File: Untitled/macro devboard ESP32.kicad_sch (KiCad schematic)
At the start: 48 parts, among them J1 12402012E212A, J2 Conn_01x02_Pin, J3 Conn_02x04_Odd_Even, Q1 BSS84LT1G, SW1 MX_SW_HS, SW3 RST, SW6 MX_SW_HS, SW7 MX_SW_HS, SW8 MX_SW_HS, SW9 MX_SW_HS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

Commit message: used keypad, which doesn't work
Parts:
- removed J2: Conn_01x02_Pin, Connector_JST:JST_XH_B2B-XH-A_1x02_P2.50mm_Vertical, symbol Connector:Conn_01x02_Pin
- added C1: 100nF, Capacitor_SMD:C_0603_1608Metric_Pad1.08x0.95mm_HandSolder, symbol Device:C
- added J4: Conn_01x02_Pin, Connector_JST:JST_PH_S2B-PH-K_1x02_P2.00mm_Horizontal, symbol Connector:Conn_01x02_Pin
- added SW2: 1825232-1, 1825232-1:1825232-1_TEC, symbol 2025-07-25_23-02-08:OS102011MA1QN1
- added TP1: VBAT, TestPoint:TestPoint_Pad_D2.0mm, symbol Connector:TestPoint
- added TP2: GND, TestPoint:TestPoint_Pad_D2.0mm, symbol Connector:TestPoint
- added TP3: EN, TestPoint:TestPoint_Pad_D2.0mm, symbol Connector:TestPoint
- added TP4: VBUS, TestPoint:TestPoint_Pad_D2.0mm, symbol Connector:TestPoint
- added TP5: VDD, TestPoint:TestPoint_Pad_D2.0mm, symbol Connector:TestPoint
- added TP6: VIN, TestPoint:TestPoint_Pad_D2.0mm, symbol Connector:TestPoint
- R14: value 2.7k -> PROG
- SW1, SW6, SW7, SW8, SW9: footprint keyswitches:Kailh_socket_MX -> keyswitches:Kailh_socket_MX_optional
- U4: footprint Package_TO_SOT_SMD:SOT-23-5 -> Package_TO_SOT_SMD:SC-74A-5_1.55x2.9mm_P0.95mm
- renumbered JP11 to LED0, JP10 to LED1
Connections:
- net EN: now also TP3.1
- net GND: now also C1.2, J4.2 (Pin_2), TP2.1
- net VBAT: now also SW2.1, SW2.2
- net VBUS: now also C1.1, TP4.1
- net VDD: now also TP5.1
- net at C3.2, C4.2, D11.1 (K)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: now also TP6.1
- new net VBAT_IN: J4.1 (Pin_1), SW2.3, TP1.1
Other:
- note added: "A compact 2X3 macro pad devboard, powered by the ESP32-C3. FEATURES: - 5 key switches, 1 rotary encoder - 8 accessible IO header pins - 2 controllable LEDs (optional) - USB-C interface, with ESD protection - Battery Charging"
- note added: "Battery Charging Management"
- note added: "IO"
- note added: "Mounting"
- note removed: "This is a macro-pad that also works as a dev board, based on the nRF52840 to teach myself about Quarq's HW workflow. FEATURES: - 6 key switches, 1 rotary encoder - 26 accessible IO header pins - USB-C interface, with ESD protection - Antenna"
- moved on the sheet: C8, C9, D10, D12, D8, D9, H1, H2, J1, J3, LED0, LED1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

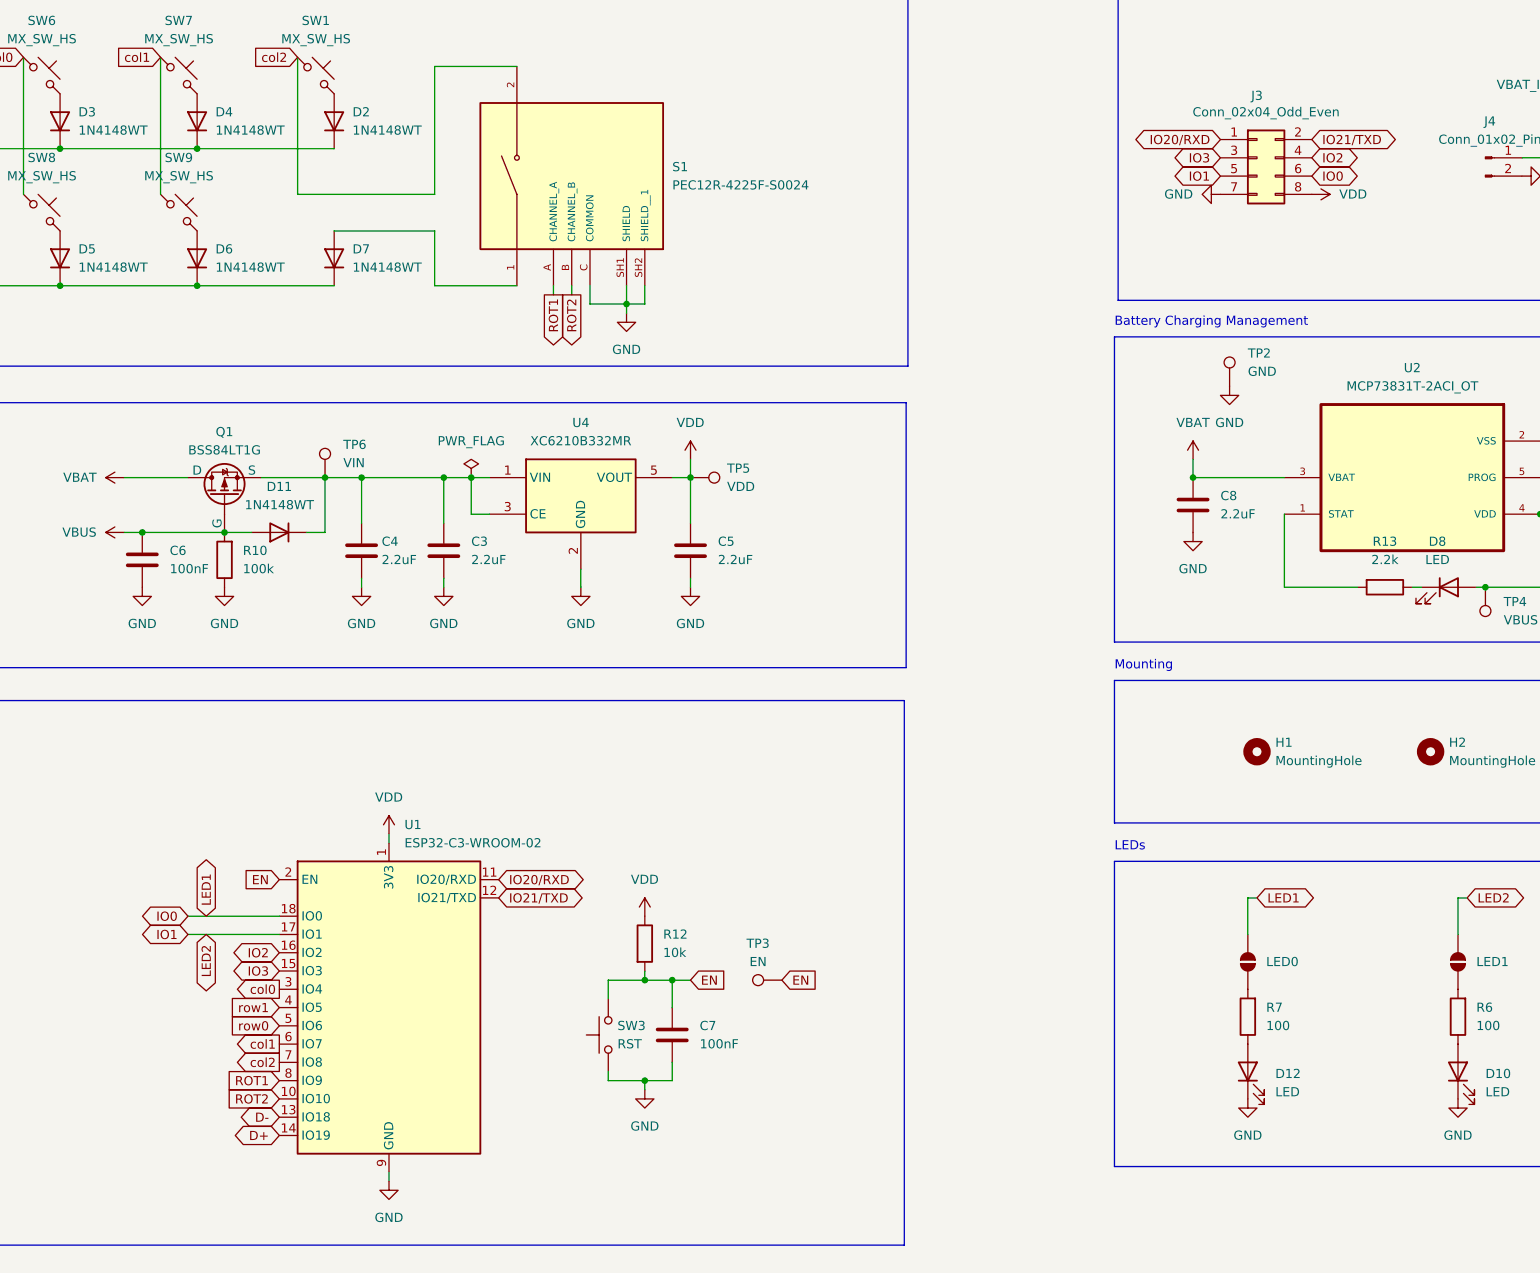
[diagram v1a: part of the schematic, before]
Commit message: fixed GPIOs for SPI
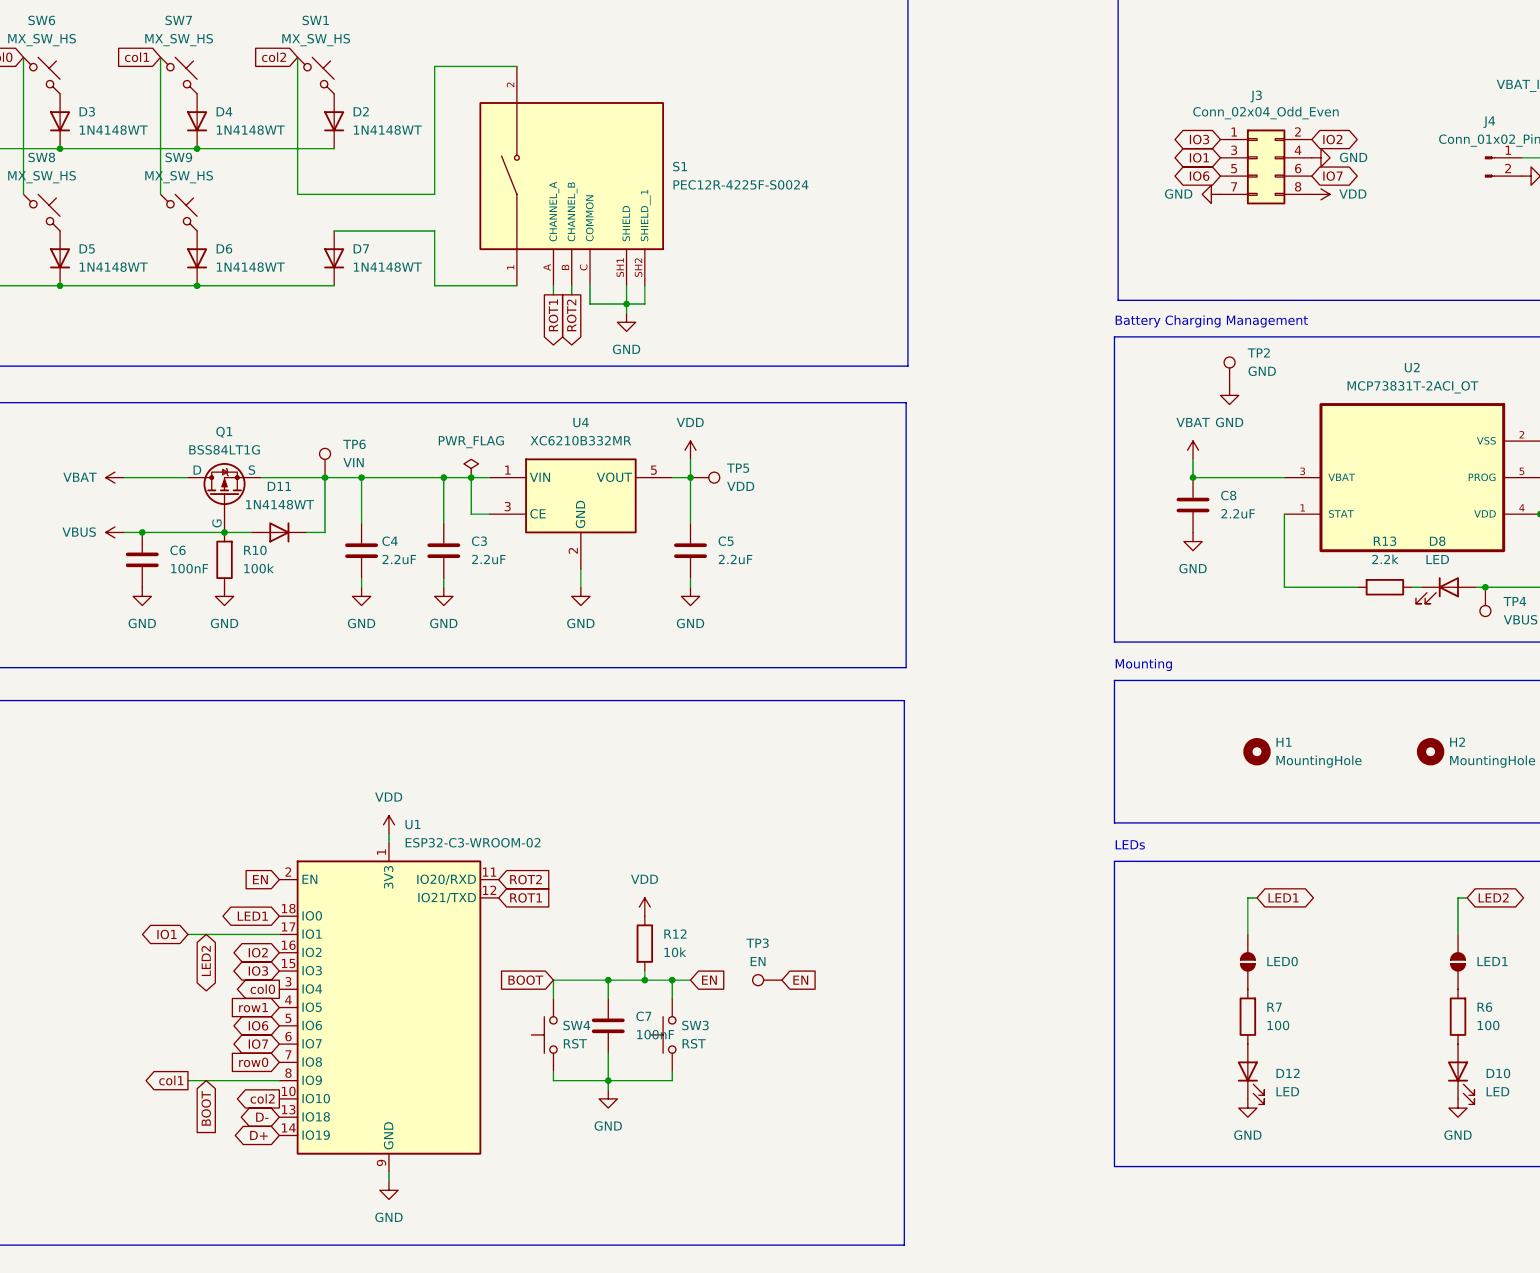
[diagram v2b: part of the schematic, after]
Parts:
- added SW4: RST, Button_Switch_SMD:SW_Tactile_SPST_NO_Straight_CK_PTS636Sx25SMTRLFS, symbol Switch:SW_Push
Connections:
- net GND: now also J3.4 (Pin_4), SW4.1
- net IO1: now also J3.3 (Pin_3); no longer J3.5 (Pin_5)
- net IO2: now also J3.2 (Pin_2); no longer J3.4 (Pin_4)
- net IO3: now also J3.1 (Pin_1); no longer J3.3 (Pin_3)
- net ROT1: now also U1.12 (IO21/TXD); no longer U1.8 (IO9)
- net ROT2: now also U1.11 (IO20/RXD); no longer U1.10 (IO10)
- net col2: now also U1.10 (IO10); no longer U1.7 (IO8)
- net row0: now also U1.7 (IO8); no longer U1.5 (IO6)
- net EN renamed BOOT
- net BOOT: now also SW7.1, SW9.1, U1.8 (IO9), SW4.2
- net IO0 renamed LED1
- net LED1: no longer J3.6 (Pin_6)
- removed net IO20/RXD: J3.1 (Pin_1), U1.11 (IO20/RXD)
- removed net IO21/TXD: J3.2 (Pin_2), U1.12 (IO21/TXD)
- removed net col1: SW7.1, SW9.1, U1.6 (IO7)
- new net IO6: J3.5 (Pin_5), U1.5 (IO6)
- new net IO7: J3.6 (Pin_6), U1.6 (IO7)
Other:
- moved on the sheet: C7, SW3
